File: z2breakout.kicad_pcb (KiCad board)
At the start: 2 copper layers, 42 x 26 mm, 16 parts, among them K1 CONN_3, P1 Z2DOCK, P2 CONN_5, P3 CONN_4, P4 CONN_3X2, P5 CONN_9X2

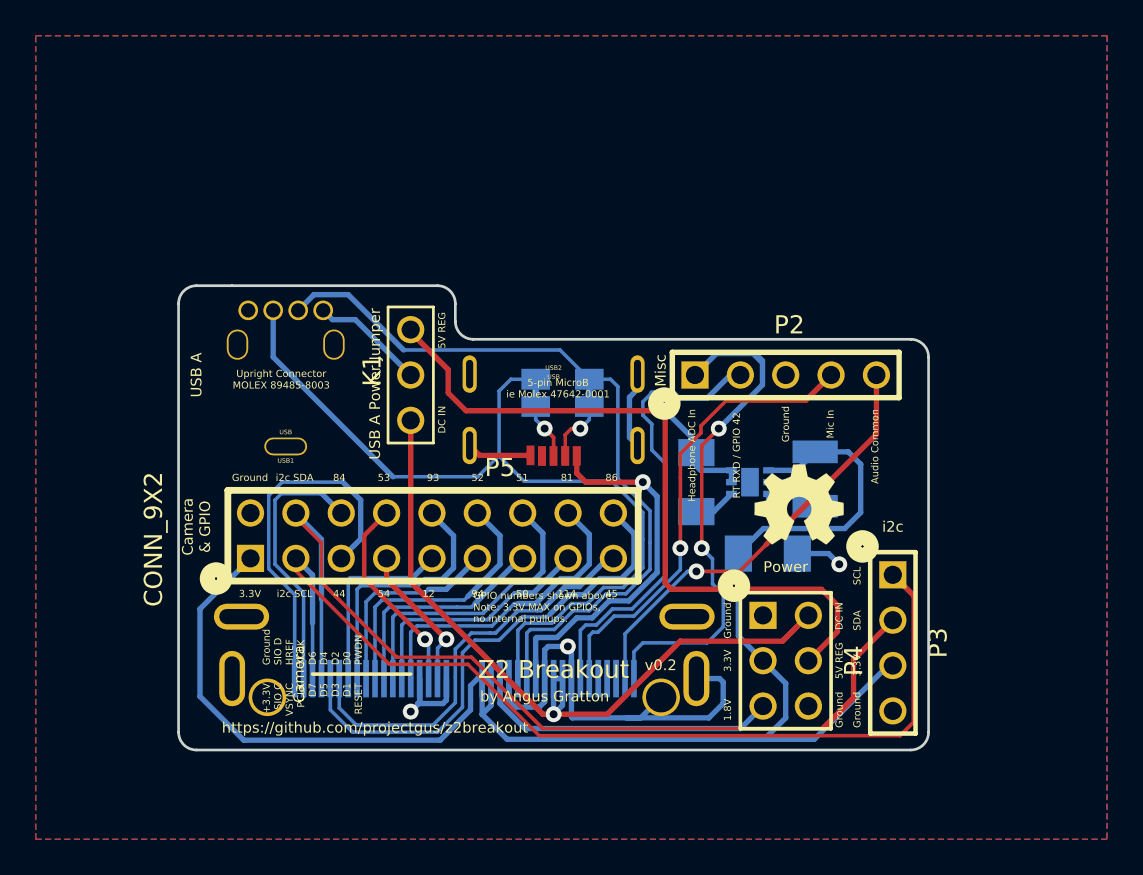
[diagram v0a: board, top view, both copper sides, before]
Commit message: Reroute with correct pin order, better connector spacing
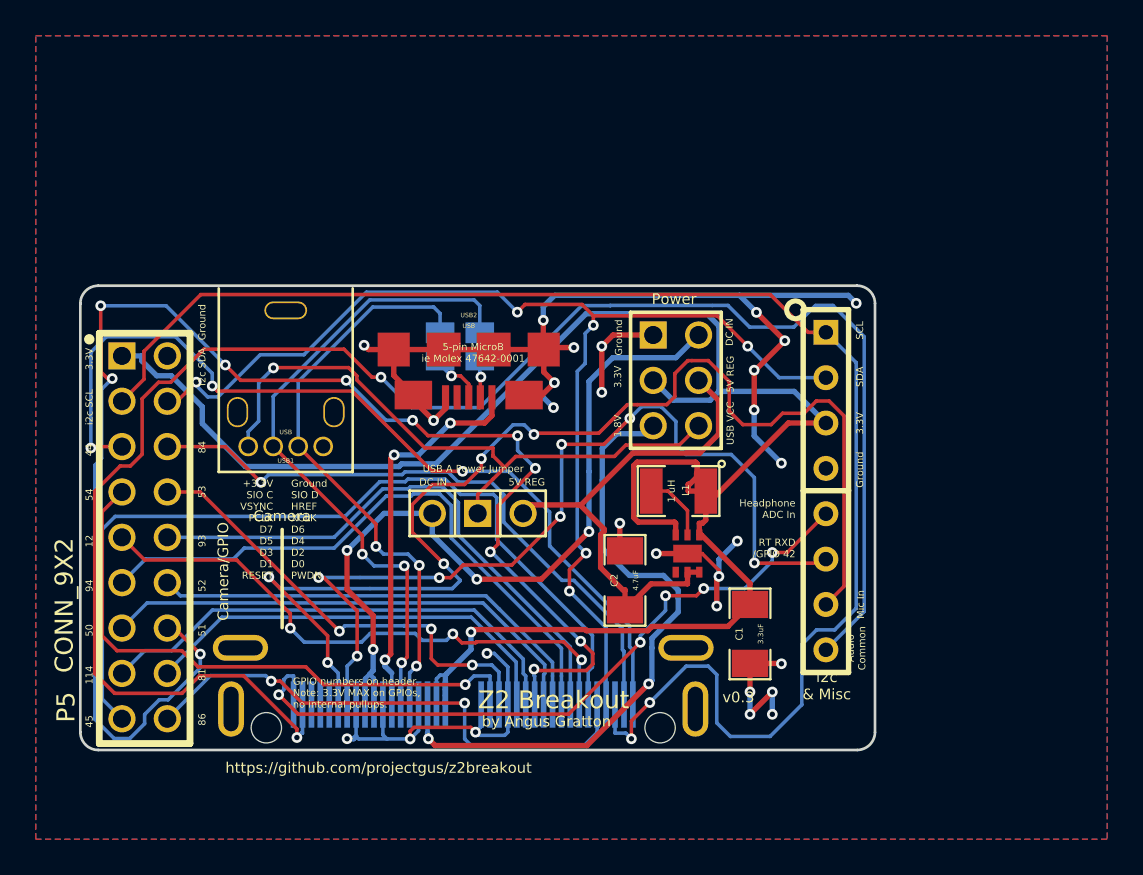
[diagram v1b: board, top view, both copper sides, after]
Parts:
- removed G***: LOGO_OSHW_silkscreen_5mm, LOGO_OSHW_silkscreen_5mm
- removed G***: LOGO_OSHW_silkscreen_2mm, LOGO_OSHW_silkscreen_2mm
- removed P3: CONN_4, PIN_ARRAY_4x1
- C1, C2, L1, REG1: moved to F.Cu
- P2: value CONN_5 -> CONN_8; footprint PIN_ARRAY_5x1 -> SIL-8
- USB2: footprint USBMICROB_MOLEX_47642-0001 -> USBMICROB_HIROSE_ZX62_B_5PA
- moved P5 20.3 mm to (191.1, 146.9), turned to 270 degrees
- moved P4 16.9 mm to (220.8, 134.3)
- moved K1 8.61 mm to (209.8, 141.8), turned to 180 degrees
- moved L1 7.68 mm to (221.0, 140.5), turned to 180 degrees
- moved P2 6.88 mm to (229.2, 140.5), turned to 270 degrees
- moved C2 6.80 mm to (218.0, 145.5), turned to 90 degrees
- moved JP2 6.66 mm to (209.9, 132.4)
- moved JP1 5.95 mm to (207.6, 132.4)
- moved USB2 5.76 mm to (209.2, 135.2), turned to 180 degrees
- moved REG1 5.32 mm to (221.5, 144.0), turned to 90 degrees
- moved C1 4.61 mm to (225.0, 148.5), turned to 270 degrees
- moved P1 1.71 mm to (208.9, 152.7)
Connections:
- K1 pad 1: /DC_IN -> /REG_5V
- K1 pad 3: /REG_5V -> /DC_IN
- P1 pad : GND -> (no net)
- P1 pad SH: GND -> (no net)
- P2 pad 1: /ADC_IN -> /I2C_SCL
- P2 pad 2: /BTRXD_GP42 -> /I2C_SDA
- P2 pad 3: GND -> /3V3
- P2 pad 4: /MIC_IN -> GND
- P2 pad 5: /AUDIO_COMMON -> /ADC_IN
- P4 pad 6: GND -> /USB_VCC
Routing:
- net /AUDIO_COMMON: track 28.3 -> 98.2 mm, vias 1 -> 2
- net /CAM_D2_GP51: track 20.4 -> 84.0 mm, vias 0 -> 11
- net GND: track 45.2 -> 100.8 mm, vias 3 -> 27
- net /MIC_IN: track 26.0 -> 68.7 mm, vias 1 -> 5
- net /USB_VCC: track 6.40 -> 35.7 mm, vias 0 -> 1
- net /CAM_LV_GP44: track 24.2 -> 50.4 mm, vias 0 -> 3
- net /GP45: track 23.0 -> 48.7 mm
- net /BTRXD_GP42: track 25.4 -> 50.4 mm, vias 0 -> 7
- net /CAM_PCLK_GP54: track 8.33 -> 33.2 mm
- net /I2C_SCL: track 62.3 -> 85.5 mm, vias 0 -> 2
- net /CAM_D5_GP94: track 11.5 -> 34.5 mm
- net /CAM_D7_GP12: track 10.7 -> 32.4 mm, vias 0 -> 3
- net /1V8: track 17.2 -> 36.0 mm, vias 0 -> 2
- net /3V3: track 88.6 -> 107.3 mm, vias 0 -> 1
- net /REG_5V: track 47.1 -> 28.8 mm, vias 1 -> 0
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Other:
- board size 42 x 26 mm -> 44.5 x 26 mm
- net class Default: clearance 0.15 -> 0.2; via_dia 0.889 -> 0.6; via_drill 0.635 -> 0.3
- net class Power: clearance 0.15 -> 0.2; via_dia 0.889 -> 0.6; via_drill 0.635 -> 0.3
- rule trace_clearance: 0.15 -> 0.2
- rule trace_min: 0.15 -> 0.2
- rule via_min_drill: 0.508 -> 0.3
- rule via_min_size: 0.889 -> 0.6
- board text added: "Camera/GPIO"
- board text added: "GPIO numbers on header. Note: 3.3V MAX on GPIOs, no internal pullups."
- board text added: "RT RXD /GPIO 42"
- board text added: "USB VCC"
- board text added: "i2c & Misc"
- board text added: "v0.3"
- board text removed: "C1 3.3uF"
- board text removed: "C2 4.7uF"
- board text removed: "Camera & GPIO"
- board text removed: "GPIO numbers shown above. Note: 3.3V MAX on GPIOs, no internal pullups."
- board text removed: "Hirose ST60X-36S"
- board text removed: "L1 1 uH"
- board text removed: "Misc"
- board text removed: "RT RXD / GPIO 42"
- board text removed: "TPS61240"
- board text removed: "USB A"
- board text removed: "Upright Connector MOLEX 89485-8003"
- board text removed: "i2c"
- board text removed: "v0.2"

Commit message: Fix up silkscreen, try to improve grounding
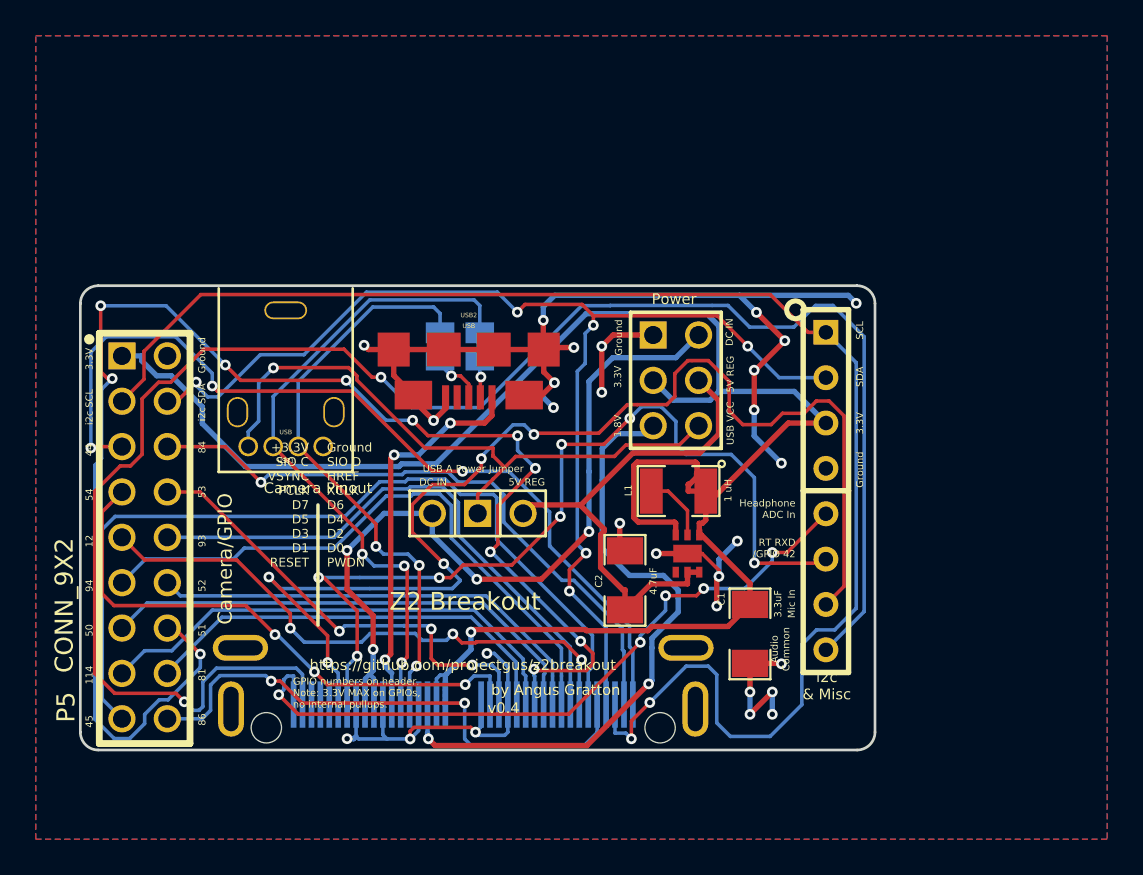
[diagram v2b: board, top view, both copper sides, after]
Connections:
- P1 pad SH: (no net) -> GND
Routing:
- net /CAM_PCLK_GP54: track 33.2 -> 31.8 mm, vias 1 -> 3
- net /SSPRXD2_GP86: track 29.7 -> 30.5 mm
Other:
- board text added: "(C) Angus Gratton 2013 TAPR Open Hardware License V1.0"
- board text added: "Camera Pinout"
- board text added: "v0.4"
- board text removed: "5-pin MicroB ie Molex 47642-0001"
- board text removed: "Camera"
- board text removed: "TAPR Open Hardware License V1.0"
- board text removed: "v0.3"

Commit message: Clean up silkscreen a bit, add i2c pullup resistors
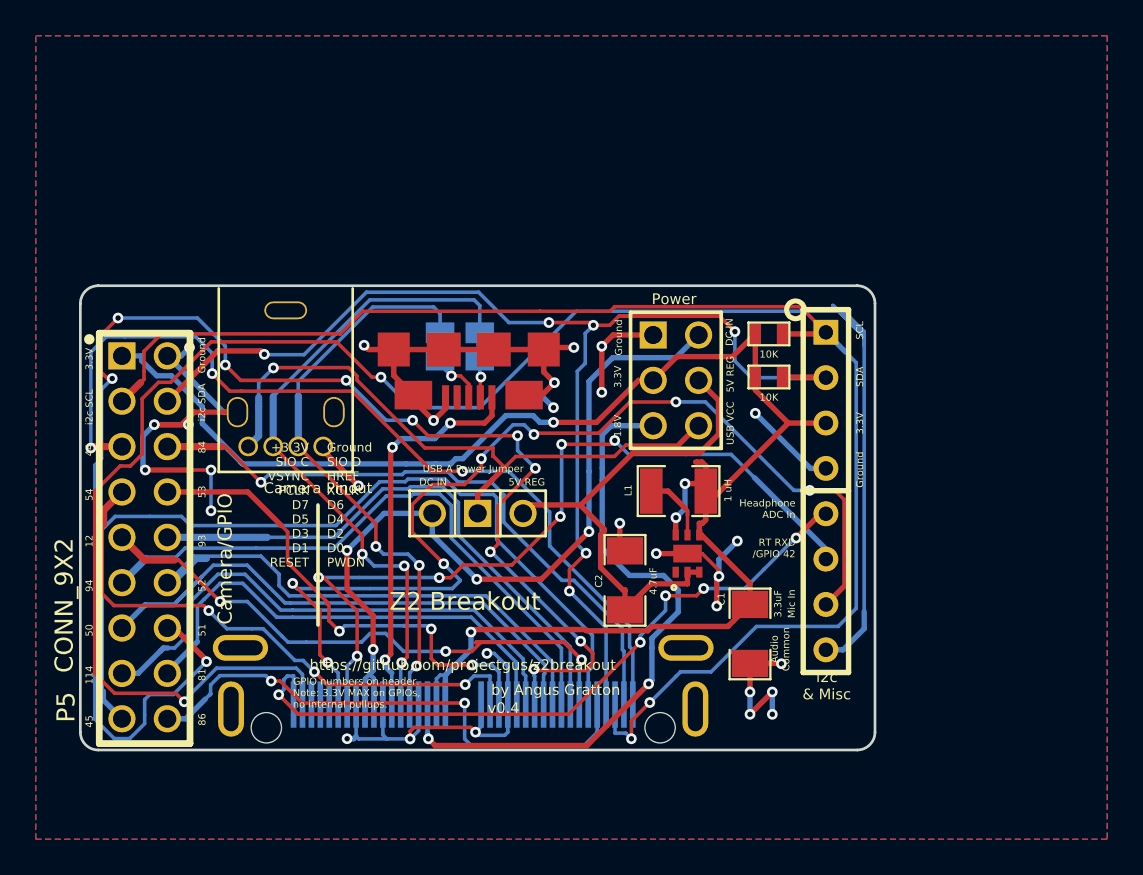
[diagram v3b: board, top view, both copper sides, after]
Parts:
- added R1: 10K, SM0603, F.Cu at (226.1, 134.1)
- added R2: 10K, SM0603, F.Cu at (226.1, 131.7)
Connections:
- P1 pad 3: N-0000029 -> (no net)
- P1 pad 4: N-0000032 -> (no net)
- P1 pad 5: N-0000031 -> (no net)
- P1 pad SH: GND -> (no net)
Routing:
- net /3V3: track 107.3 -> 94.8 mm, vias 1 -> 4
- net /MIC_IN: track 68.7 -> 58.9 mm, vias 5 -> 7
- net /I2C_SDA: track 66.1 -> 74.0 mm
- net /CAM_D7_GP12: track 32.4 -> 38.4 mm
- net /BTRXD_GP42: track 50.4 -> 45.4 mm, vias 7 -> 6
- net /I2C_SCL: track 85.5 -> 80.6 mm
- net /CAM_D4_GP52: track 25.8 -> 30.1 mm
- net /AUDIO_COMMON: track 98.4 -> 102.5 mm
- net /CAM_D3_GP50: track 27.9 -> 31.8 mm
- net /CAM_D0_GP81: track 24.3 -> 27.1 mm
- net /CAM_D1_GP114: track 27.7 -> 30.3 mm
- net /CAM_MCLK_GP53: track 25.8 -> 27.5 mm
- net GND: track 100.8 -> 99.1 mm, vias 27 -> 28
- net N-000007: track 3.84 -> 5.05 mm
